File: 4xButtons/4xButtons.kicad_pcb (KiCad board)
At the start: 2 copper layers, 20.3 x 18.3 mm, 12 parts, among them J1 Conn_01x01_Male, J2 Conn_01x01_Male, J3 Conn_01x01_Male, J4 Conn_01x01_Male, J5 Conn_01x01_Male, J6 Conn_01x01_Male, J7 Conn_01x01_Male, J8 Conn_01x01_Male, SW1 SW_Push, SW2 SW_Push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

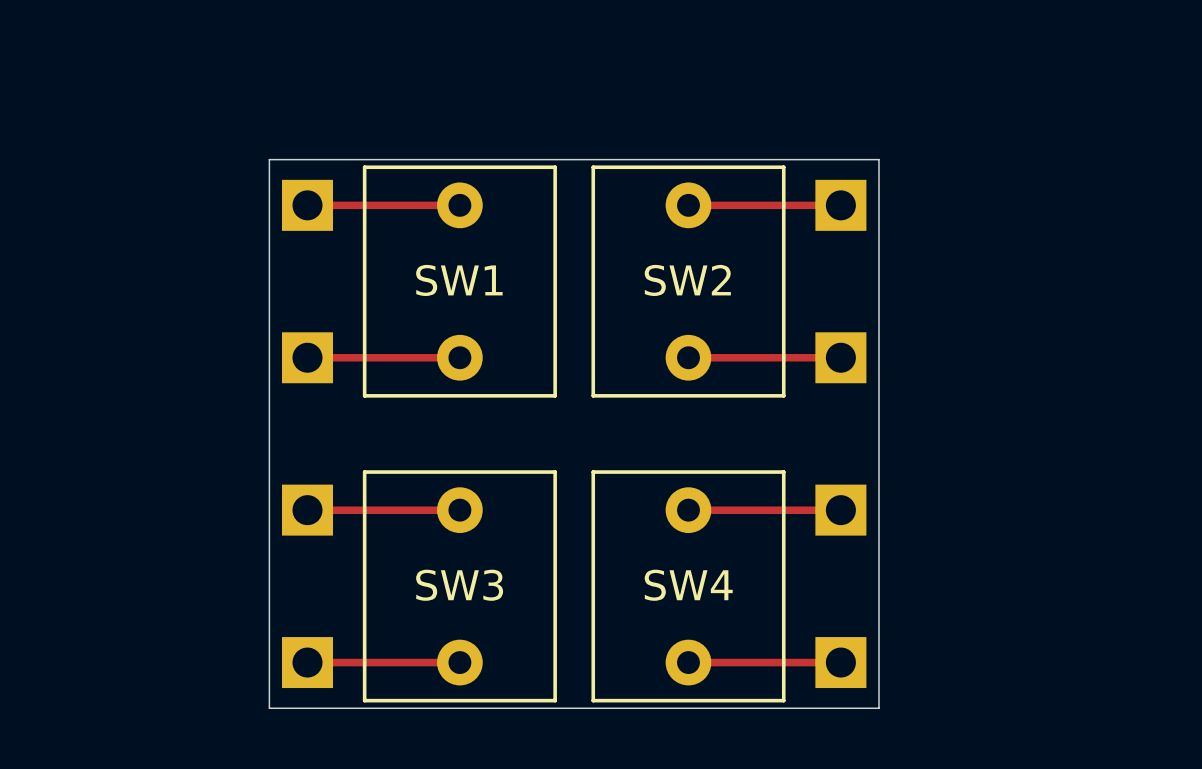
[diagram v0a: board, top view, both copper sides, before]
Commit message: Change sheet size to 8.5x11
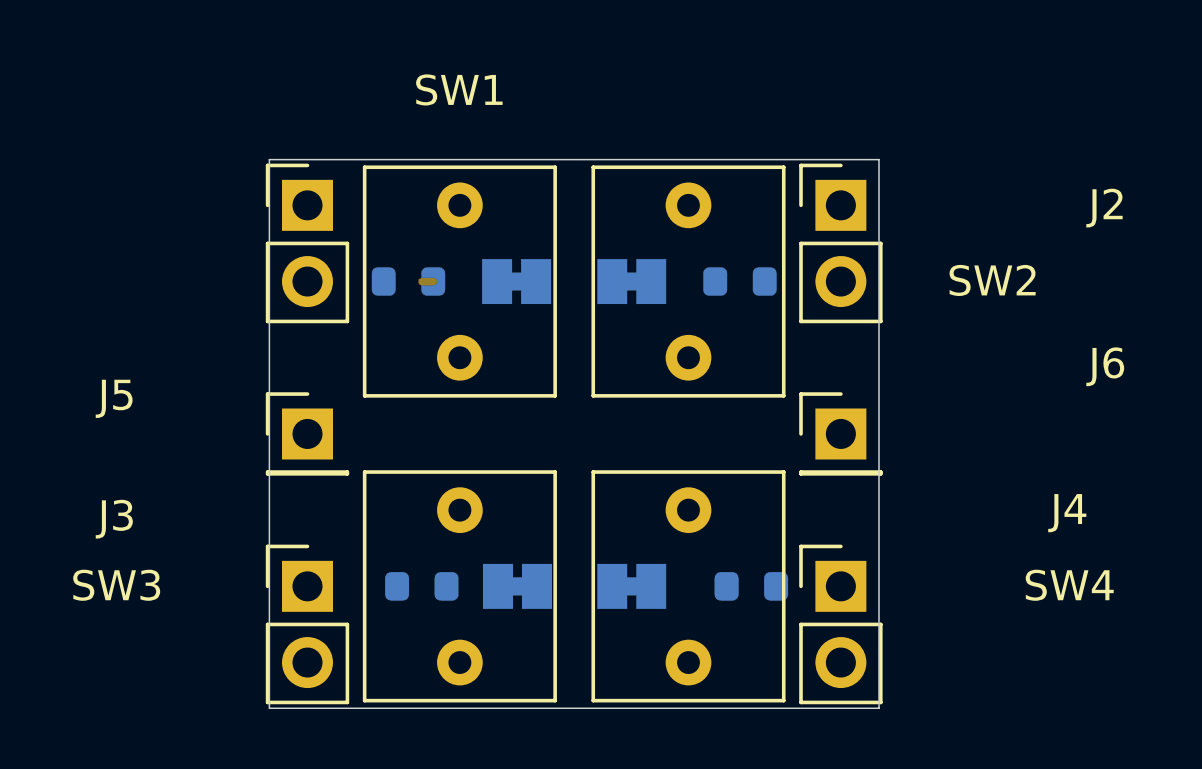
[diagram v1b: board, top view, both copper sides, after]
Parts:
- removed J7, J8: Conn_01x01_Male, Connector_PinHeader_2.54mm:PinHeader_1x01_P2.54mm_Vertical
- added JP1: Jumper_2_Bridged, Jumper:SolderJumper-2_P1.3mm_Bridged_Pad1.0x1.5mm, B.Cu at (146.7, 104.1)
- added JP2: Jumper_2_Bridged, Jumper:SolderJumper-2_P1.3mm_Bridged_Pad1.0x1.5mm, B.Cu at (150.5, 104.1)
- added JP3: Jumper_2_Bridged, Jumper:SolderJumper-2_P1.3mm_Bridged_Pad1.0x1.5mm, B.Cu at (146.7, 114.3)
- added JP4: Jumper_2_Bridged, Jumper:SolderJumper-2_P1.3mm_Bridged_Pad1.0x1.5mm, B.Cu at (150.5, 114.3)
- added R1: 1k, Resistor_SMD:R_0603_1608Metric, B.Cu at (143.1, 104.1)
- added R2: 1k, Resistor_SMD:R_0603_1608Metric, B.Cu at (154.1, 104.1)
- added R3: 1k, Resistor_SMD:R_0603_1608Metric, B.Cu at (143.5, 114.3)
- added R4: 1k, Resistor_SMD:R_0603_1608Metric, B.Cu at (154.5, 114.3)
- J1, J2, J3, J4: value Conn_01x01_Male -> Conn_01x02_Male; footprint Connector_PinHeader_2.54mm:PinHeader_1x01_P2.54mm_Vertical -> Connector_PinHeader_2.54mm:PinHeader_1x02_P2.54mm_Vertical; moved to F.Cu
- J5, J6: moved to F.Cu
- moved J5 19.3 mm to (139.7, 109.2)
- moved J2 18.5 mm to (157.5, 101.6)
- moved J4 18.0 mm to (157.5, 114.3)
- moved J6 2.54 mm to (157.5, 109.2)
- moved J3 2.54 mm to (139.7, 114.3)
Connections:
- SW1 pad 2: Net-(J2-Pad1) -> Net-(J1-Pad2)
- SW2 pad 1: Net-(J7-Pad1) -> Net-(J2-Pad2)
- SW2 pad 2: Net-(J8-Pad1) -> Net-(J2-Pad1)
- SW3 pad 2: Net-(J4-Pad1) -> Net-(J3-Pad2)
- SW4 pad 1: Net-(J5-Pad1) -> Net-(J4-Pad2)
- SW4 pad 2: Net-(J6-Pad1) -> Net-(J4-Pad1)
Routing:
- net Net-(J4-Pad1): track 5.08 -> 0.00 mm
- net Net-(J3-Pad1): track 5.08 -> 0.00 mm
- net Net-(J2-Pad1): track 5.08 -> 0.00 mm
- net Net-(J1-Pad1): track 5.08 -> 0.00 mm
- net Net-(J8-Pad1): track 5.08 -> 0.00 mm
- net Net-(J7-Pad1): track 5.08 -> 0.00 mm
- net Net-(J6-Pad1): track 5.08 -> 0.00 mm
- net Net-(J5-Pad1): track 5.08 -> 0.00 mm
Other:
- net class Default removed
